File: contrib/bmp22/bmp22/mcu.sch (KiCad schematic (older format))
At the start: 47 parts, among them J301 USB_C_Receptacle_USB2.0, J302 Conn_ARM_JTAG_SWD_10, SW301 SW_DIP_x01, U301 USBLC6-2SC6, U302 STM32F103CBUx, Y301 8MHz

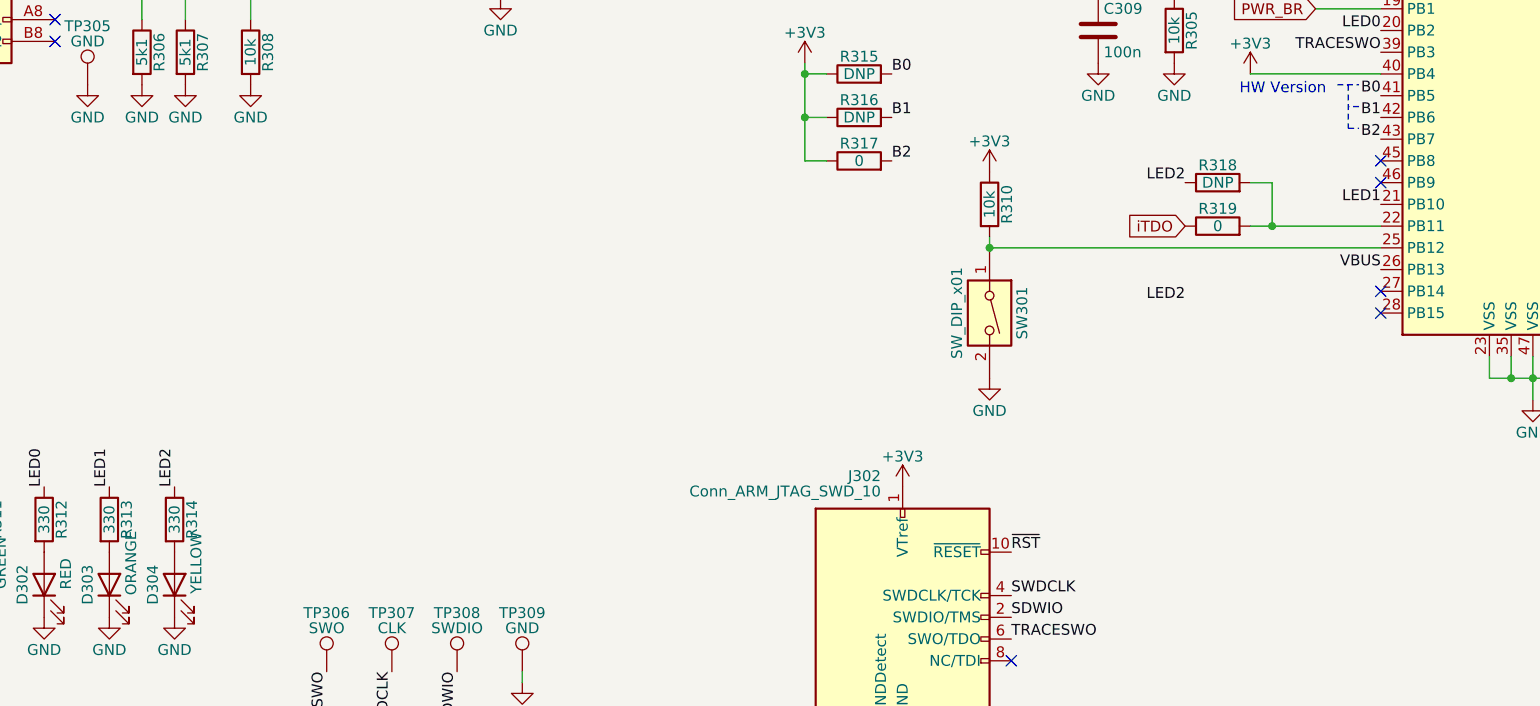
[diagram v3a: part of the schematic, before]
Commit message: layouted new changes, added keepout for tag connect, improved gnd plane
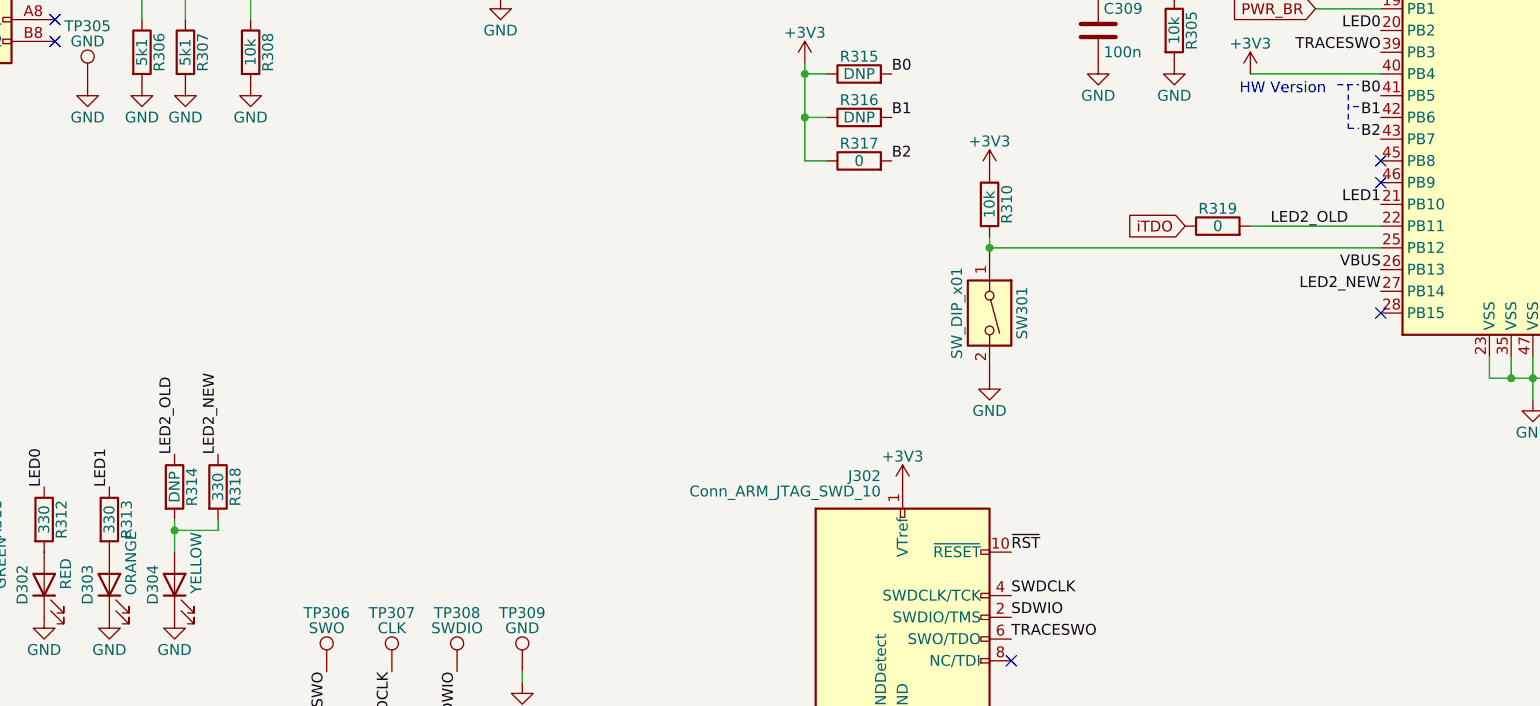
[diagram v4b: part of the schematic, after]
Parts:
- R314: value 330 -> DNP
- R318: value DNP -> 330
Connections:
- net LED2_OLD: now reaches R319.2, U302.22 (PB11)
- net LED2_OLD: now also R314.1; no longer R318.2
- net LED2_NEW: now reaches U302.27 (PB14)
- net LED2_NEW: now also R318.1
- net at D304.2 (A), R314.2: now also R318.2
- removed net LED2: R314.1, R318.1
- no-connect marks 12 -> 11
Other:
- moved on the sheet: R314
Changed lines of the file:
@@
 Text Label 8000 4950 2    50   ~ 0
 LED1
-Text Label 7100 4850 2    50   ~ 0
-LED2
+Text Label 2650 6100 1    50   ~ 0
+LED2_NEW
 $Comp
 L Device:R R310
@@
 Text Label 8000 5250 2    50   ~ 0
 VBUS
-NoConn ~ 8000 5350
 NoConn ~ 8000 5450
 Text Label 1850 6250 1    50   ~ 0
@@
 Text Label 2150 6250 1    50   ~ 0
 LED1
-Text Label 2450 6250 1    50   ~ 0
-LED2
 $Comp
 L Device:LED D301
@@
 L Device:R R314
 U 1 1 5F2F8AD0
-P 2450 6400
-F 0 "R314" V 2530 6400 50  0000 C CNN
-F 1 "330" V 2450 6400 50  0000 C CNN
-F 2 "Resistor_SMD:R_0402_1005Metric" V 2380 6400 50  0001 C CNN
-F 3 "~" H 2450 6400 50  0001 C CNN
-	1    2450 6400
+P 2450 6250
+F 0 "R314" V 2530 6250 50  0000 C CNN
+F 1 "DNP" V 2450 6250 50  0000 C CNN
+F 2 "Resistor_SMD:R_0402_1005Metric" V 2380 6250 50  0001 C CNN
+F 3 "~" H 2450 6250 50  0001 C CNN
+	1    2450 6250
 	1    0    0    -1
 $EndComp
@@
 	0    -1   -1   0
 $EndComp
-Wire Wire Line
-	7400 5050 7500 5050
-$Comp
-L Device:R R318
-U 1 1 5F16E85C
-P 7250 4850
-F 0 "R318" V 7330 4850 50  0000 C CNN
-F 1 "DNP" V 7250 4850 50  0000 C CNN
-F 2 "Resistor_SMD:R_0402_1005Metric" V 7180 4850 50  0001 C CNN
-F 3 "~" H 7250 4850 50  0001 C CNN
-	1    7250 4850
-	0    -1   -1   0
-$EndComp
-Wire Wire Line
-	7400 4850 7500 4850
-Wire Wire Line
-	7500 4850 7500 5050
-Connection ~ 7500 5050
-Wire Wire Line
-	7500 5050 8000 5050
-Text Label 7100 5400 2    50   ~ 0
-LED2
+Text Label 7850 5050 2    50   ~ 0
+LED2_OLD
 $Comp
 L Device:R R317
@@
 Text Label 5750 4750 0    50   ~ 0
 B2
+Wire Wire Line
+	5350 4300 5350 4350
+Wire Wire Line
+	5350 4750 5450 4750
+Wire Wire Line
+	5450 4550 5350 4550
+Connection ~ 5350 4550
+Wire Wire Line
+	5350 4550 5350 4750
+Wire Wire Line
+	5450 4350 5350 4350
+Connection ~ 5350 4350
+Wire Wire Line
+	5350 4350 5350 4550
+Wire Wire Line
+	7400 5050 8000 5050
+Text Label 2450 6100 1    50   ~ 0
+LED2_OLD
+$Comp
+L Device:R R318
+U 1 1 5F1D4066
+P 2650 6250
+F 0 "R318" V 2730 6250 50  0000 C CNN
+F 1 "330" V 2650 6250 50  0000 C CNN
+F 2 "Resistor_SMD:R_0402_1005Metric" V 2580 6250 50  0001 C CNN
+F 3 "~" H 2650 6250 50  0001 C CNN
+	1    2650 6250
+	1    0    0    -1
+$EndComp
+Wire Wire Line
+	2450 6550 2450 6450
+Wire Wire Line
+	2650 6400 2650 6450
+Wire Wire Line
+	2650 6450 2450 6450
+Connection ~ 2450 6450
+Wire Wire Line
+	2450 6450 2450 6400
+Text Label 8000 5350 2    50   ~ 0
+LED2_NEW
 $Comp
 L power:+3V3 #PWR0332
@@
 	1    0    0    -1
 $EndComp
-Wire Wire Line
-	5350 4300 5350 4350
-Wire Wire Line
-	5350 4750 5450 4750
-Wire Wire Line
-	5450 4550 5350 4550
-Connection ~ 5350 4550
-Wire Wire Line
-	5350 4550 5350 4750
-Wire Wire Line
-	5450 4350 5350 4350
-Connection ~ 5350 4350
-Wire Wire Line
-	5350 4350 5350 4550
 $EndSCHEMATC

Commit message: updated schematic and layout
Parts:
- removed R315, R316: DNP, Resistor_SMD:R_0402_1005Metric, symbol Device:R
- removed R317, R319: 0, Resistor_SMD:R_0402_1005Metric, symbol Device:R
- removed R318: 330, Resistor_SMD:R_0402_1005Metric, symbol Device:R
- R314: value DNP -> 330
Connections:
- net B0 is gone; now on net +3V3: U302.41 (PB5)
- net B1 is gone; now on net +3V3: U302.42 (PB6)
- net LED2_NEW: no longer names the net of U302.27 (PB14)
- net LED2_OLD renamed LED2
- no-connect marks 11 -> 12
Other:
- moved on the sheet: R314
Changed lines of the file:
@@
 Text Label 8000 4150 2    50   ~ 0
 LED0
-Text Notes 7350 4450 0    50   ~ 0
+Text Notes 7400 4650 0    50   ~ 0
 HW Version
 NoConn ~ 8000 4750
@@
 Text Label 8000 4950 2    50   ~ 0
 LED1
-Text Label 2650 6100 1    50   ~ 0
-LED2_NEW
 $Comp
 L Device:R R310
@@
 P 2150 6700
 F 0 "D303" H 2150 6800 50  0000 C CNN
-F 1 "ORANGE" H 2250 6600 50  0000 C CNN
+F 1 "ORANGE" H 2200 6600 50  0000 C CNN
 F 2 "LED_SMD:LED_0603_1608Metric" H 2150 6700 50  0001 C CNN
 F 3 "~" H 2150 6700 50  0001 C CNN
@@
 P 2450 6700
 F 0 "D304" H 2450 6800 50  0000 C CNN
-F 1 "YELLOW" H 2550 6600 50  0000 C CNN
+F 1 "YELLOW" H 2550 6550 50  0000 C CNN
 F 2 "LED_SMD:LED_0603_1608Metric" H 2450 6700 50  0001 C CNN
 F 3 "~" H 2450 6700 50  0001 C CNN
@@
 L Device:R R314
 U 1 1 5F2F8AD0
-P 2450 6250
-F 0 "R314" V 2530 6250 50  0000 C CNN
-F 1 "DNP" V 2450 6250 50  0000 C CNN
-F 2 "Resistor_SMD:R_0402_1005Metric" V 2380 6250 50  0001 C CNN
-F 3 "~" H 2450 6250 50  0001 C CNN
-	1    2450 6250
+P 2450 6400
+F 0 "R314" V 2530 6400 50  0000 C CNN
+F 1 "330" V 2450 6400 50  0000 C CNN
+F 2 "Resistor_SMD:R_0402_1005Metric" V 2380 6400 50  0001 C CNN
+F 3 "~" H 2450 6400 50  0001 C CNN
+	1    2450 6400
 	1    0    0    -1
 $EndComp
@@
 L power:+3V3 #PWR0329
 U 1 1 5F315565
-P 7400 4350
-F 0 "#PWR0329" H 7400 4200 50  0001 C CNN
-F 1 "+3V3" H 7400 4490 50  0000 C CNN
-F 2 "" H 7400 4350 50  0001 C CNN
-F 3 "" H 7400 4350 50  0001 C CNN
-	1    7400 4350
+P 7400 4300
+F 0 "#PWR0329" H 7400 4150 50  0001 C CNN
+F 1 "+3V3" H 7400 4440 50  0000 C CNN
+F 2 "" H 7400 4300 50  0001 C CNN
+F 3 "" H 7400 4300 50  0001 C CNN
+	1    7400 4300
 	1    0    0    -1
 $EndComp
@@
 	1    3750 7100
 	1    0    0    -1
-$EndComp
-Text GLabel 7100 5050 0    50   Input ~ 0
-iTDO
-$Comp
-L Device:R R319
-U 1 1 5F1694D2
-P 7250 5050
-F 0 "R319" V 7330 5050 50  0000 C CNN
-F 1 "0" V 7250 5050 50  0000 C CNN
-F 2 "Resistor_SMD:R_0402_1005Metric" V 7180 5050 50  0001 C CNN
-F 3 "~" H 7250 5050 50  0001 C CNN
-	1    7250 5050
-	0    -1   -1   0
-$EndComp
-Text Label 7850 5050 2    50   ~ 0
-LED2_OLD
-$Comp
-L Device:R R317
-U 1 1 5F17213D
-P 5600 4750
-F 0 "R317" V 5680 4750 50  0000 C CNN
-F 1 "0" V 5600 4750 50  0000 C CNN
-F 2 "Resistor_SMD:R_0402_1005Metric" V 5530 4750 50  0001 C CNN
-F 3 "~" H 5600 4750 50  0001 C CNN
-	1    5600 4750
-	0    -1   -1   0
-$EndComp
-$Comp
-L Device:R R316
-U 1 1 5F1733D8
-P 5600 4550
-F 0 "R316" V 5680 4550 50  0000 C CNN
-F 1 "DNP" V 5600 4550 50  0000 C CNN
-F 2 "Resistor_SMD:R_0402_1005Metric" V 5530 4550 50  0001 C CNN
-F 3 "~" H 5600 4550 50  0001 C CNN
-	1    5600 4550
-	0    -1   -1   0
-$EndComp
-$Comp
-L Device:R R315
-U 1 1 5F175D2C
-P 5600 4350
-F 0 "R315" V 5680 4350 50  0000 C CNN
-F 1 "DNP" V 5600 4350 50  0000 C CNN
-F 2 "Resistor_SMD:R_0402_1005Metric" V 5530 4350 50  0001 C CNN
-F 3 "~" H 5600 4350 50  0001 C CNN
-	1    5600 4350
-	0    -1   -1   0
 $EndComp
 $Comp
@@
 Wire Notes Line
 	7900 4500 7850 4500
+Text Label 2450 6250 1    50   ~ 0
+LED2
+Wire Wire Line
+	8000 4450 7400 4450
+Wire Wire Line
+	7400 4450 7400 4350
+Connection ~ 7400 4350
+Wire Wire Line
+	7400 4300 7400 4350
+Wire Wire Line
+	7400 4450 7400 4550
+Wire Wire Line
+	7400 4550 8000 4550
+Connection ~ 7400 4450
 Wire Notes Line
-	7800 4400 7900 4400
-Text Label 5750 4350 0    50   ~ 0
-B0
-Text Label 5750 4550 0    50   ~ 0
-B1
-Text Label 5750 4750 0    50   ~ 0
-B2
-Wire Wire Line
-	5350 4300 5350 4350
-Wire Wire Line
-	5350 4750 5450 4750
-Wire Wire Line
-	5450 4550 5350 4550
-Connection ~ 5350 4550
-Wire Wire Line
-	5350 4550 5350 4750
-Wire Wire Line
-	5450 4350 5350 4350
-Connection ~ 5350 4350
-Wire Wire Line
-	5350 4350 5350 4550
-Wire Wire Line
-	7400 5050 8000 5050
-Text Label 2450 6100 1    50   ~ 0
-LED2_OLD
-$Comp
-L Device:R R318
-U 1 1 5F1D4066
-P 2650 6250
-F 0 "R318" V 2730 6250 50  0000 C CNN
-F 1 "330" V 2650 6250 50  0000 C CNN
-F 2 "Resistor_SMD:R_0402_1005Metric" V 2580 6250 50  0001 C CNN
-F 3 "~" H 2650 6250 50  0001 C CNN
-	1    2650 6250
-	1    0    0    -1
-$EndComp
-Wire Wire Line
-	2450 6550 2450 6450
-Wire Wire Line
-	2650 6400 2650 6450
-Wire Wire Line
-	2650 6450 2450 6450
-Connection ~ 2450 6450
-Wire Wire Line
-	2450 6450 2450 6400
-Text Label 8000 5350 2    50   ~ 0
-LED2_NEW
-$Comp
-L power:+3V3 #PWR0332
-U 1 1 5F192667
-P 5350 4300
-F 0 "#PWR0332" H 5350 4150 50  0001 C CNN
-F 1 "+3V3" H 5350 4440 50  0000 C CNN
-F 2 "" H 5350 4300 50  0001 C CNN
-F 3 "" H 5350 4300 50  0001 C CNN
-	1    5350 4300
-	1    0    0    -1
-$EndComp
+	7850 4400 7900 4400
+Text Label 8000 5050 2    50   ~ 0
+LED2
+NoConn ~ 8000 5350
 $EndSCHEMATC
